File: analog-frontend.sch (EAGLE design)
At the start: 67 parts, among them IC1 ADG731, IC2 TPS63031, IC3 INA332, IC4 OPA2320, IC5 TM4C123G, IC6 NRF24L01SMD, Y1 CRYSTAL3X2, Y2 CRYSTAL3X2

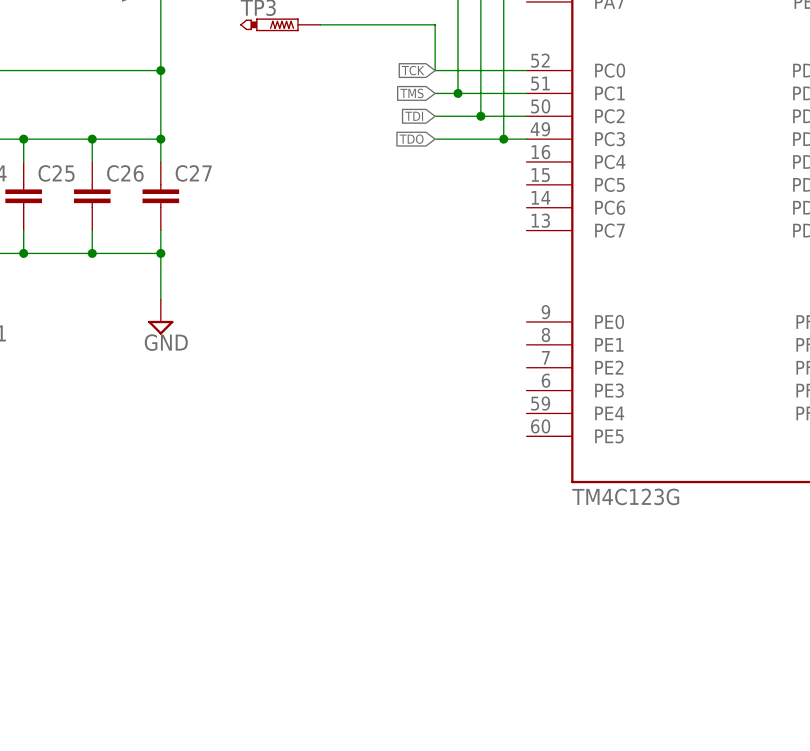
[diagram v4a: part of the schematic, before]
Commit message: added signal planes
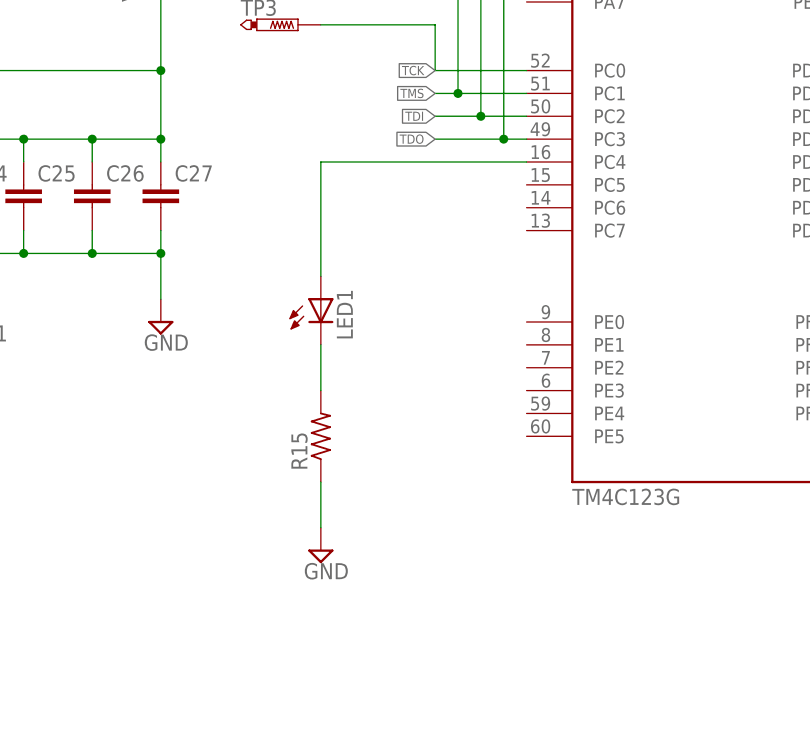
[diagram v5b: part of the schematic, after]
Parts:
- added LED1: (no value), ng:LED0402
- added R15: (no value), rcl:R-US_R0201
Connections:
- new net N$63: IC5A.PC4, LED1.A
- new net N$66: LED1.C, R15.2
- net GND: now also R15.1
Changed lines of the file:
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@@
 <part name="R14" library="rcl" deviceset="R-US_" device="R0201"/>
 <part name="SUPPLY11" library="supply2" deviceset="GND" device="" value="GNDA"/>
+<part name="LED1" library="ng" deviceset="LED" device="0402"/>
+<part name="R15" library="rcl" deviceset="R-US_" device="R0201"/>
+<part name="SUPPLY25" library="supply2" deviceset="GND" device=""/>
 </parts>
 <sheets>
@@
 <instance part="R14" gate="G$1" x="223.52" y="243.84" rot="R90"/>
 <instance part="SUPPLY11" gate="GND" x="139.7" y="175.26"/>
+<instance part="LED1" gate="G$1" x="149.86" y="81.28"/>
+<instance part="R15" gate="G$1" x="149.86" y="68.58" rot="R90"/>
+<instance part="SUPPLY25" gate="GND" x="149.86" y="55.88"/>
 </instances>
 <busses>
@@
 <pinref part="SUPPLY23" gate="GND" pin="GND"/>
 <wire x1="93.98" y1="119.38" x2="93.98" y2="124.46" width="0.1524" layer="91"/>
+</segment>
+<segment>
+<pinref part="R15" gate="G$1" pin="1"/>
+<pinref part="SUPPLY25" gate="GND" pin="GND"/>
+<wire x1="149.86" y1="58.42" x2="149.86" y2="63.5" width="0.1524" layer="91"/>
 </segment>
 </net>
@@
 </segment>
 </net>
+<net name="N$63" class="0">
+<segment>
+<pinref part="IC5" gate="A" pin="PC4"/>
+<pinref part="LED1" gate="G$1" pin="A"/>
+<wire x1="172.72" y1="99.06" x2="149.86" y2="99.06" width="0.1524" layer="91"/>
+<wire x1="149.86" y1="99.06" x2="149.86" y2="86.36" width="0.1524" layer="91"/>
+</segment>
+</net>
+<net name="N$66" class="0">
+<segment>
+<pinref part="LED1" gate="G$1" pin="C"/>
+<pinref part="R15" gate="G$1" pin="2"/>
+<wire x1="149.86" y1="78.74" x2="149.86" y2="73.66" width="0.1524" layer="91"/>
+</segment>
+</net>

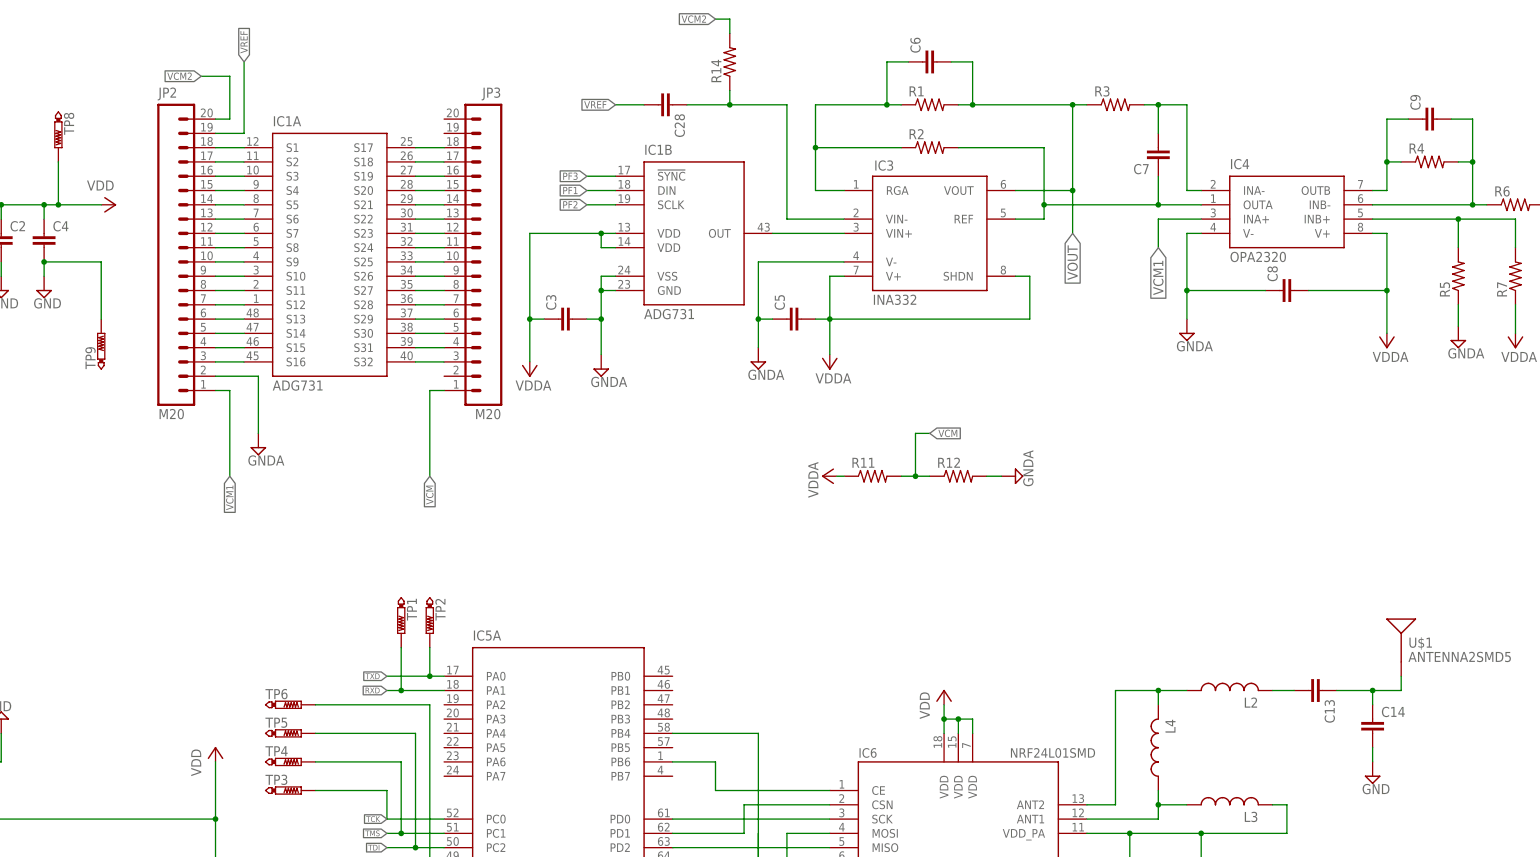
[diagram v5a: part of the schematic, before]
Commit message: fixed analog input connection
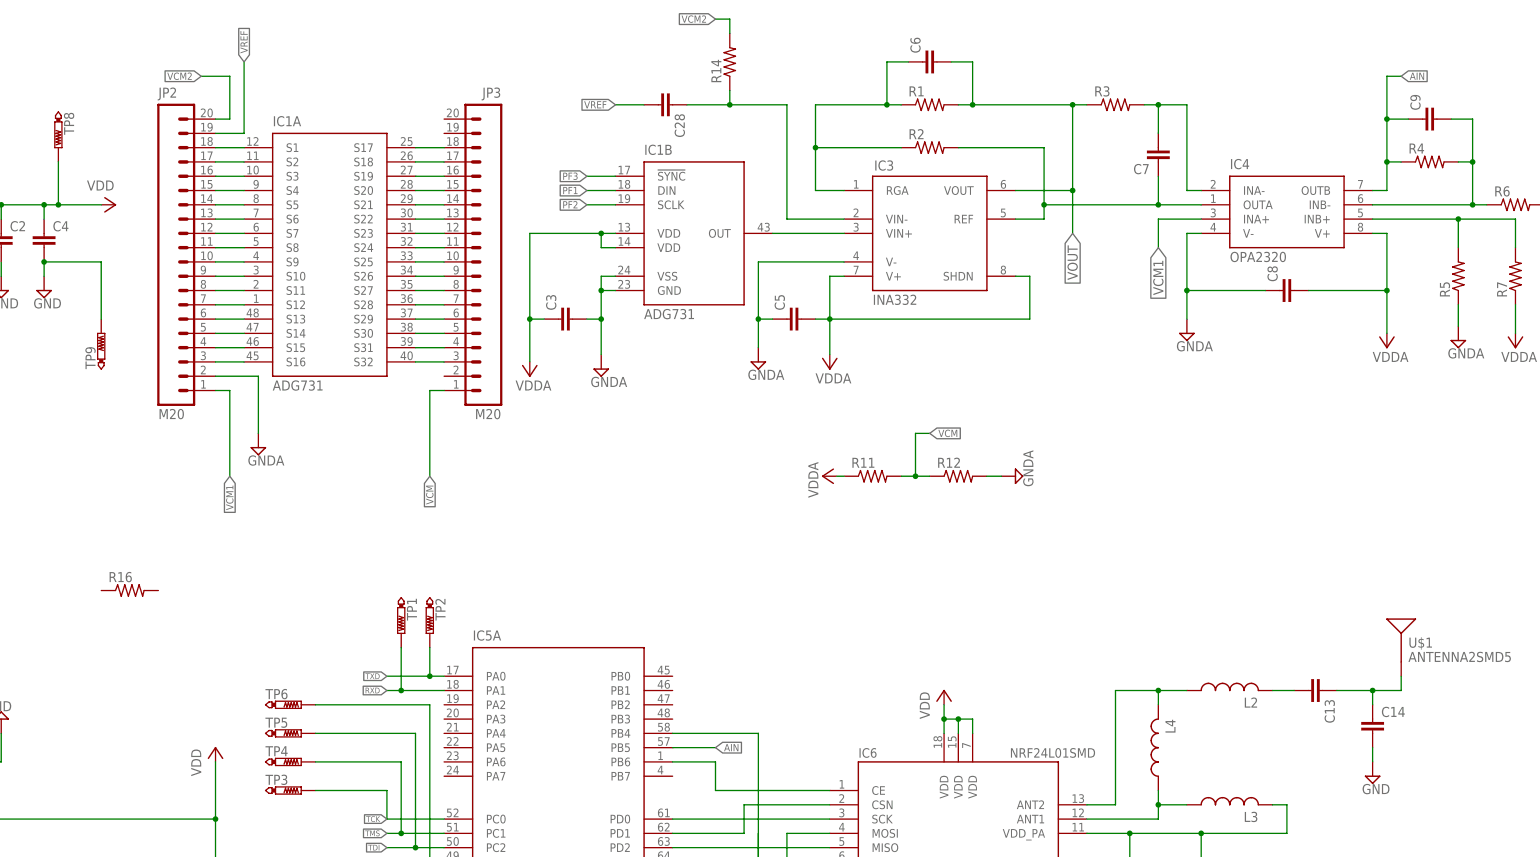
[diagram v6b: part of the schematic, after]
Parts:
- added R16: (no value), FAB_Hello:RESISTOR0402
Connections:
- removed net N$41: C9.1, IC4.OUTB, R4.1
- new net AIN: C9.1, IC4.OUTB, IC5A.PB5, R4.1
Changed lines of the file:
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@@
 <setting verticaltext="up"/>
 </settings>
-<grid distance="0.1" unitdist="inch" unit="inch" style="lines" multiple="1" display="yes" altdistance="0.05" altunitdist="inch" altunit="inch"/>
+<grid distance="0.1" unitdist="inch" unit="inch" style="lines" multiple="1" display="no" altdistance="0.01" altunitdist="inch" altunit="inch"/>
 <layers>
 <layer number="1" name="Top" color="4" fill="1" visible="no" active="no"/>
@@
 <part name="R15" library="rcl" deviceset="R-US_" device="R0201"/>
 <part name="SUPPLY25" library="supply2" deviceset="GND" device=""/>
+<part name="R16" library="FAB_Hello" deviceset="RESISTOR" device="0402"/>
 </parts>
 <sheets>
@@
 <instance part="R15" gate="G$1" x="149.86" y="68.58" rot="R90"/>
 <instance part="SUPPLY25" gate="GND" x="149.86" y="55.88"/>
+<instance part="R16" gate="G$1" x="116.84" y="149.86"/>
 </instances>
 <busses>
@@
 </segment>
 </net>
-<net name="N$41" class="0">
+<net name="AIN" class="0">
 <segment>
 <pinref part="R4" gate="G$1" pin="1"/>
@@
 <wire x1="340.36" y1="233.68" x2="340.36" y2="226.06" width="0.1524" layer="91"/>
 <junction x="340.36" y="226.06"/>
-</segment>
-</net>
+<wire x1="340.36" y1="233.68" x2="340.36" y2="241.3" width="0.1524" layer="91"/>
+<junction x="340.36" y="233.68"/>
+<wire x1="340.36" y1="241.3" x2="342.9" y2="241.3" width="0.1524" layer="91"/>
+<label x="342.9" y="241.3" size="1.27" layer="95" xref="yes"/>
+</segment>
+<segment>
+<pinref part="IC5" gate="A" pin="PB5"/>
+<wire x1="213.36" y1="121.92" x2="220.98" y2="121.92" width="0.1524" layer="91"/>
+<label x="220.98" y="121.92" size="1.27" layer="95" xref="yes"/>
+</segment>
+</net>

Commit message: Revert "fixed analog input connection"
This reverts commit 9ace190f50edbfe5c6ebec0060ae9832deedc051.
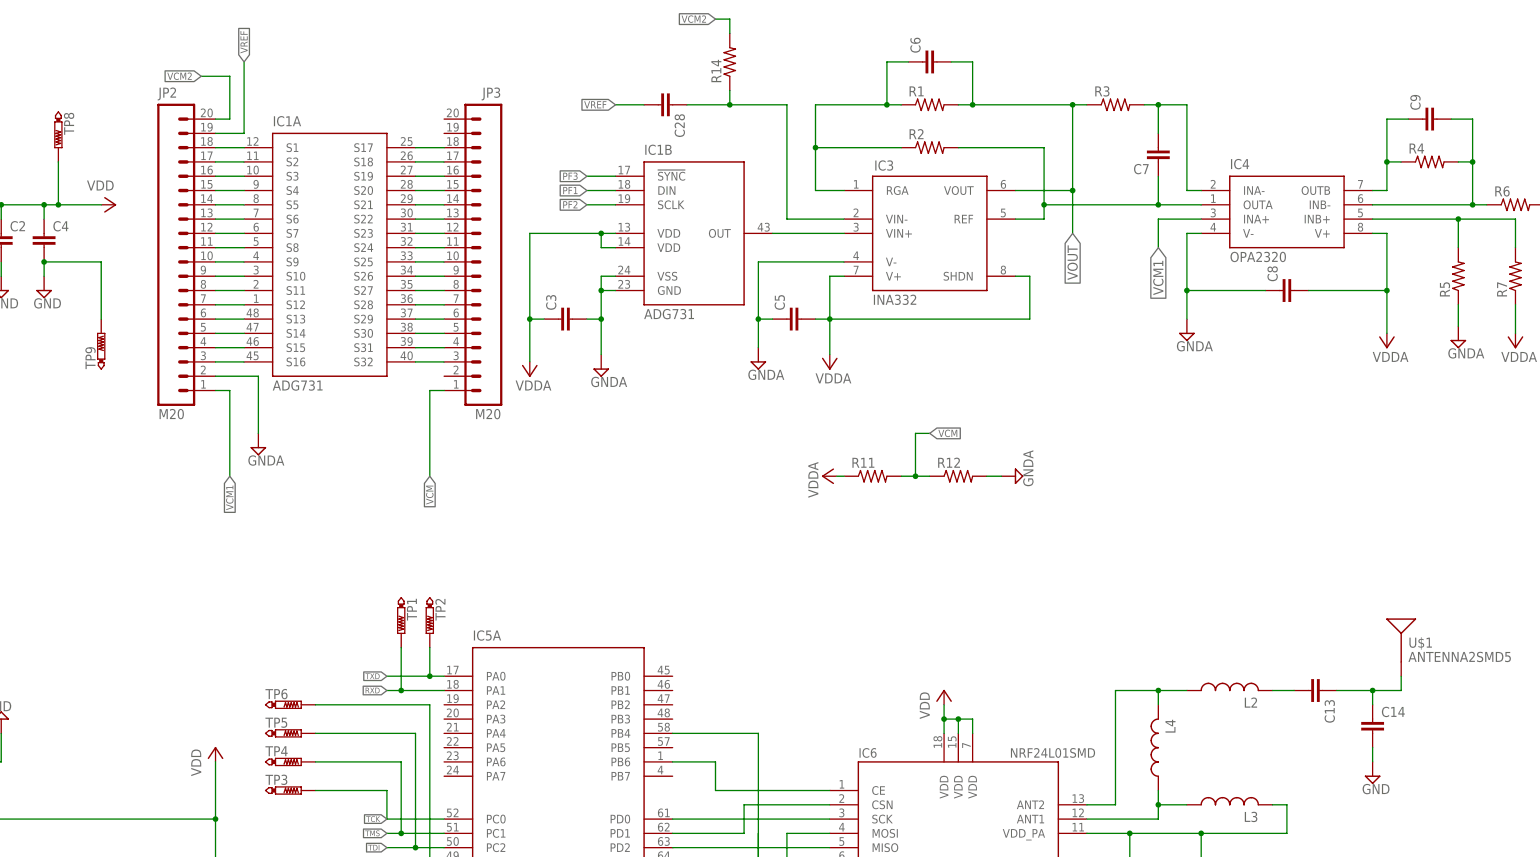
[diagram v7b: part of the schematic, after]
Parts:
- removed R16: (no value), FAB_Hello:RESISTOR0402
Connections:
- removed net AIN: C9.1, IC4.OUTB, IC5A.PB5, R4.1
- new net N$41: C9.1, IC4.OUTB, R4.1
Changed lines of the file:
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@@
 <setting verticaltext="up"/>
 </settings>
-<grid distance="0.1" unitdist="inch" unit="inch" style="lines" multiple="1" display="no" altdistance="0.01" altunitdist="inch" altunit="inch"/>
+<grid distance="0.1" unitdist="inch" unit="inch" style="lines" multiple="1" display="yes" altdistance="0.05" altunitdist="inch" altunit="inch"/>
 <layers>
 <layer number="1" name="Top" color="4" fill="1" visible="no" active="no"/>
@@
 <part name="R15" library="rcl" deviceset="R-US_" device="R0201"/>
 <part name="SUPPLY25" library="supply2" deviceset="GND" device=""/>
-<part name="R16" library="FAB_Hello" deviceset="RESISTOR" device="0402"/>
 </parts>
 <sheets>
@@
 <instance part="R15" gate="G$1" x="149.86" y="68.58" rot="R90"/>
 <instance part="SUPPLY25" gate="GND" x="149.86" y="55.88"/>
-<instance part="R16" gate="G$1" x="116.84" y="149.86"/>
 </instances>
 <busses>
@@
 </segment>
 </net>
-<net name="AIN" class="0">
+<net name="N$41" class="0">
 <segment>
 <pinref part="R4" gate="G$1" pin="1"/>
@@
 <wire x1="340.36" y1="233.68" x2="340.36" y2="226.06" width="0.1524" layer="91"/>
 <junction x="340.36" y="226.06"/>
-<wire x1="340.36" y1="233.68" x2="340.36" y2="241.3" width="0.1524" layer="91"/>
-<junction x="340.36" y="233.68"/>
-<wire x1="340.36" y1="241.3" x2="342.9" y2="241.3" width="0.1524" layer="91"/>
-<label x="342.9" y="241.3" size="1.27" layer="95" xref="yes"/>
-</segment>
-<segment>
-<pinref part="IC5" gate="A" pin="PB5"/>
-<wire x1="213.36" y1="121.92" x2="220.98" y2="121.92" width="0.1524" layer="91"/>
-<label x="220.98" y="121.92" size="1.27" layer="95" xref="yes"/>
-</segment>
-</net>
+</segment>
+</net>
